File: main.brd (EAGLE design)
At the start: 42.9 x 27.9 mm, 46 parts, among them IC1 MEGA8-AI, IC2 MCP73831, IC3 7805DT, Q2 32768k

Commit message: Firmware
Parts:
- moved R12 86.6 mm to (34.3, 19.1)
- moved R14 82.4 mm to (21.6, 24.1), turned to 180 degrees
- moved T5 80.7 mm to (30.5, 17.1), turned to 180 degrees
- moved R15 75.6 mm to (5.08, 15.2), turned to 270 degrees
- moved T4 73.2 mm to (26.7, 17.8), turned to 180 degrees
- moved R11 70.4 mm to (21.6, 19.1), turned to 180 degrees
- moved R13 65.9 mm to (8.89, 24.1)
- moved R18 56.7 mm to (21.6, 26.7), turned to 180 degrees
- moved R16 55.8 mm to (21.6, 16.5)
- moved R19 52.6 mm to (11.4, 26.7)
- moved R17 48.6 mm to (16.5, 26.7), turned to 180 degrees
- turned T6 to 90 degrees
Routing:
- net N$5: track 0.00 -> 5.61 mm

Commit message: Schematics
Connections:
- net N$38: now also IC1.19; no longer IC1.12
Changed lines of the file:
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@@
 </signal>
 <signal name="N$38">
-<contactref element="IC1" pad="12"/>
 <contactref element="R22" pad="1"/>
 <contactref element="S1" pad="1"/>
+<contactref element="IC1" pad="19"/>
+<wire x1="3.0988" y1="11.1506" x2="23.565" y2="2.0574" width="0" layer="19" extent="1-1"/>
 <wire x1="-42.062" y1="58.42" x2="3.0988" y2="11.1506" width="0" layer="19" extent="1-1"/>
-<wire x1="20.4724" y1="6.75" x2="3.0988" y2="11.1506" width="0" layer="19" extent="1-1"/>
 </signal>
 <signal name="N$5">

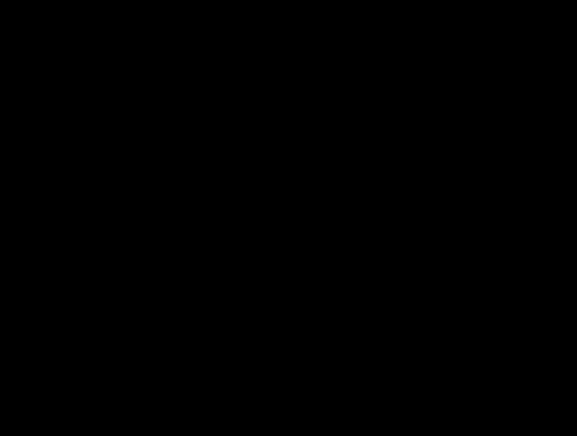
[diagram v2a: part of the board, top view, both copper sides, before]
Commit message: Button noise rejection
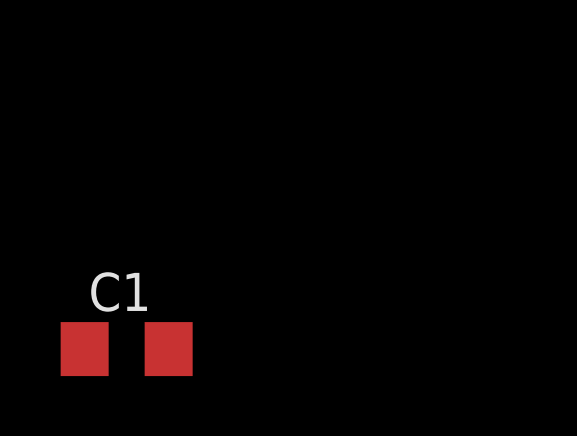
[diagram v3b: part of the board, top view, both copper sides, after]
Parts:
- added C1: 100n, rcl:C1206
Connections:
- net GND: now also C1.2
- net N$38: now also C1.1
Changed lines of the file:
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@@
 </element>
 <element name="D4" library="diode" package="D-7.5" value="" x="31.75" y="6.35" rot="R270"/>
+<element name="C1" library="rcl" package="C1206" value="100n" x="-57.15" y="-5.08"/>
 </elements>
 <signals>
@@
 <contactref element="D2" pad="A"/>
 <contactref element="S1" pad="3"/>
-<wire x1="35.56" y1="2.54" x2="3.0988" y2="6.6294" width="0" layer="19" extent="1-1"/>
-<wire x1="-45.72" y1="27.94" x2="35.56" y2="2.54" width="0" layer="19" extent="1-1"/>
+<contactref element="C1" pad="2"/>
+<wire x1="-45.72" y1="27.94" x2="-55.75" y2="-5.08" width="0" layer="19" extent="1-1"/>
 <wire x1="-38.1" y1="26.64" x2="-45.72" y2="27.94" width="0" layer="19" extent="1-1"/>
-<wire x1="14.605" y1="10.6934" x2="-38.1" y2="26.64" width="0" layer="19" extent="1-1"/>
-<wire x1="-54.48" y1="38.1" x2="35.56" y2="2.54" width="0" layer="19" extent="1-1"/>
-<wire x1="-48.13" y1="38.1" x2="-54.48" y2="38.1" width="0" layer="19" extent="1-1"/>
-<wire x1="34.795" y1="8.255" x2="-48.13" y2="38.1" width="0" layer="19" extent="1-1"/>
-<wire x1="0.27" y1="24.4" x2="34.795" y2="8.255" width="0" layer="19" extent="1-1"/>
-<wire x1="-43.332" y1="45.72" x2="34.795" y2="8.255" width="0" layer="19" extent="1-1"/>
-<wire x1="-30.35" y1="45.72" x2="0.27" y2="24.4" width="0" layer="19" extent="1-1"/>
+<wire x1="-48.13" y1="38.1" x2="-45.72" y2="27.94" width="0" layer="19" extent="1-1"/>
+<wire x1="-54.48" y1="38.1" x2="-48.13" y2="38.1" width="0" layer="19" extent="1-1"/>
+<wire x1="-43.332" y1="45.72" x2="-48.13" y2="38.1" width="0" layer="19" extent="1-1"/>
+<wire x1="-30.35" y1="45.72" x2="-43.332" y2="45.72" width="0" layer="19" extent="1-1"/>
 <wire x1="-25.27" y1="45.72" x2="-30.35" y2="45.72" width="0" layer="19" extent="1-1"/>
 <wire x1="-20.19" y1="45.72" x2="-25.27" y2="45.72" width="0" layer="19" extent="1-1"/>
-<wire x1="39.64" y1="7.255" x2="-25.27" y2="45.72" width="0" layer="19" extent="1-1"/>
 <wire x1="-36.982" y1="58.42" x2="-43.332" y2="45.72" width="0" layer="19" extent="1-1"/>
-<wire x1="20.36" y1="3.81" x2="14.605" y2="10.6934" width="0" layer="19" extent="1-1"/>
-<wire x1="25.165" y1="2.0574" x2="20.36" y2="3.81" width="0" layer="19" extent="1-1"/>
-<wire x1="24.365" y1="10.6426" x2="25.165" y2="2.0574" width="0" layer="19" extent="1-1"/>
+<wire x1="0.27" y1="24.4" x2="-20.19" y2="45.72" width="0" layer="19" extent="1-1"/>
+<wire x1="3.0988" y1="6.6294" x2="0.27" y2="24.4" width="0" layer="19" extent="1-1"/>
+<wire x1="14.605" y1="10.6934" x2="3.0988" y2="6.6294" width="0" layer="19" extent="1-1"/>
+<wire x1="20.36" y1="3.81" x2="14.605" y2="10.6934" width="0" layer="19" extent="1-16"/>
+<wire x1="25.165" y1="2.0574" x2="20.36" y2="3.81" width="0" layer="19" extent="1-16"/>
+<wire x1="24.365" y1="10.6426" x2="20.36" y2="3.81" width="0" layer="19" extent="1-16"/>
 <wire x1="25.965" y1="10.6426" x2="24.365" y2="10.6426" width="0" layer="19" extent="1-1"/>
+<wire x1="34.795" y1="8.255" x2="25.965" y2="10.6426" width="0" layer="19" extent="1-1"/>
+<wire x1="39.64" y1="7.255" x2="34.795" y2="8.255" width="0" layer="19" extent="1-1"/>
+<wire x1="35.56" y1="2.54" x2="34.795" y2="8.255" width="0" layer="19" extent="1-1"/>
 </signal>
 <signal name="+5V">
@@
 <contactref element="S1" pad="1"/>
 <contactref element="IC1" pad="19"/>
-<wire x1="3.0988" y1="11.1506" x2="23.565" y2="2.0574" width="0" layer="19" extent="1-1"/>
+<contactref element="C1" pad="1"/>
+<wire x1="3.0988" y1="11.1506" x2="-58.55" y2="-5.08" width="0" layer="19" extent="1-1"/>
+<wire x1="23.565" y1="2.0574" x2="3.0988" y2="11.1506" width="0" layer="19" extent="1-1"/>
 <wire x1="-42.062" y1="58.42" x2="3.0988" y2="11.1506" width="0" layer="19" extent="1-1"/>
 </signal>

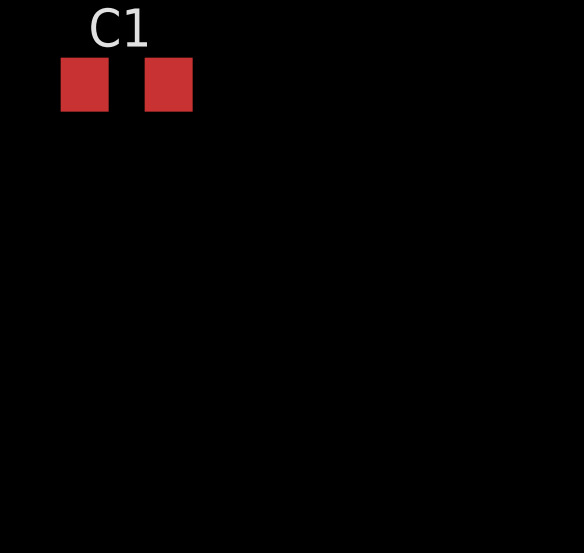
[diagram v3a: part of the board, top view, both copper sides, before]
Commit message: Pull-up resistors on TWI bus
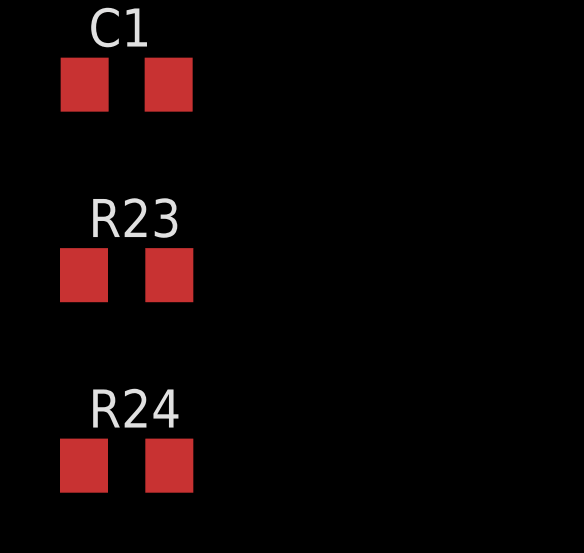
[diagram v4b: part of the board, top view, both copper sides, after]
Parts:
- added R23, R24: 4.7k, rcl:R1206
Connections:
- net +5V: now also R23.2, R24.2
- net DS1629_SCL: now also R24.1
- net DS1629_SDA: now also R23.1
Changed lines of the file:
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@@
 <element name="D4" library="diode" package="D-7.5" value="" x="31.75" y="6.35" rot="R270"/>
 <element name="C1" library="rcl" package="C1206" value="100n" x="-57.15" y="-5.08"/>
+<element name="R23" library="rcl" package="R1206" value="4.7k" x="-57.15" y="-11.43"/>
+<element name="R24" library="rcl" package="R1206" value="4.7k" x="-57.15" y="-17.78"/>
 </elements>
 <signals>
@@
 <contactref element="IC1" pad="18"/>
 <contactref element="R22" pad="2"/>
-<wire x1="-19.37" y1="62.4" x2="-14.29" y2="62.4" width="0" layer="19" extent="1-1"/>
-<wire x1="-24.45" y1="62.4" x2="-19.37" y2="62.4" width="0" layer="19" extent="1-1"/>
-<wire x1="25.72" y1="18.88" x2="-24.45" y2="62.4" width="0" layer="19" extent="1-1"/>
-<wire x1="29.53" y1="18.245" x2="25.72" y2="18.88" width="0" layer="19" extent="1-1"/>
-<wire x1="-39.218" y1="58.42" x2="29.53" y2="18.245" width="0" layer="19" extent="1-1"/>
-<wire x1="20.168" y1="19.05" x2="-39.218" y2="58.42" width="0" layer="19" extent="1-1"/>
-<wire x1="-34.138" y1="52.07" x2="20.168" y2="19.05" width="0" layer="19" extent="1-1"/>
+<contactref element="R23" pad="2"/>
+<contactref element="R24" pad="2"/>
+<wire x1="-55.728" y1="-11.43" x2="-55.728" y2="-17.78" width="0" layer="19" extent="1-1"/>
+<wire x1="-37.15" y1="29.24" x2="-55.728" y2="-11.43" width="0" layer="19" extent="1-1"/>
+<wire x1="-50.93" y1="38.1" x2="-37.15" y2="29.24" width="0" layer="19" extent="1-1"/>
+<wire x1="-57.28" y1="38.1" x2="-50.93" y2="38.1" width="0" layer="19" extent="1-1"/>
+<wire x1="-34.138" y1="52.07" x2="-50.93" y2="38.1" width="0" layer="19" extent="1-1"/>
 <wire x1="-29.058" y1="52.07" x2="-34.138" y2="52.07" width="0" layer="19" extent="1-1"/>
 <wire x1="-23.978" y1="52.07" x2="-29.058" y2="52.07" width="0" layer="19" extent="1-1"/>
-<wire x1="35.712" y1="19.05" x2="20.168" y2="19.05" width="0" layer="19" extent="1-1"/>
-<wire x1="-50.93" y1="38.1" x2="35.712" y2="19.05" width="0" layer="19" extent="1-1"/>
-<wire x1="-57.28" y1="38.1" x2="-50.93" y2="38.1" width="0" layer="19" extent="1-1"/>
-<wire x1="-37.15" y1="29.24" x2="-50.93" y2="38.1" width="0" layer="19" extent="1-1"/>
-<wire x1="25.165" y1="10.6426" x2="-37.15" y2="29.24" width="0" layer="19" extent="1-1"/>
+<wire x1="-39.218" y1="58.42" x2="-34.138" y2="52.07" width="0" layer="19" extent="1-1"/>
+<wire x1="-24.45" y1="62.4" x2="-23.978" y2="52.07" width="0" layer="19" extent="1-1"/>
+<wire x1="-19.37" y1="62.4" x2="-24.45" y2="62.4" width="0" layer="19" extent="1-1"/>
+<wire x1="-14.29" y1="62.4" x2="-19.37" y2="62.4" width="0" layer="19" extent="1-1"/>
+<wire x1="20.168" y1="19.05" x2="-23.978" y2="52.07" width="0" layer="19" extent="1-1"/>
+<wire x1="25.72" y1="18.88" x2="20.168" y2="19.05" width="0" layer="19" extent="1-1"/>
+<wire x1="29.53" y1="18.245" x2="25.72" y2="18.88" width="0" layer="19" extent="1-1"/>
+<wire x1="35.712" y1="19.05" x2="29.53" y2="18.245" width="0" layer="19" extent="1-1"/>
+<wire x1="25.165" y1="10.6426" x2="25.72" y2="18.88" width="0" layer="19" extent="1-1"/>
 <wire x1="23.565" y1="10.6426" x2="25.165" y2="10.6426" width="0" layer="19" extent="1-1"/>
 <wire x1="29.0576" y1="6.75" x2="25.165" y2="10.6426" width="0" layer="19" extent="1-1"/>
-<wire x1="24.365" y1="2.0574" x2="29.0576" y2="6.75" width="0" layer="19" extent="1-1"/>
+<wire x1="27.66" y1="1.53" x2="29.0576" y2="6.75" width="0" layer="19" extent="1-16"/>
+<wire x1="24.365" y1="2.0574" x2="27.66" y2="1.53" width="0" layer="19" extent="1-16"/>
 <wire x1="22.765" y1="2.0574" x2="24.365" y2="2.0574" width="0" layer="19" extent="1-1"/>
-<wire x1="27.66" y1="1.53" x2="22.765" y2="2.0574" width="0" layer="19" extent="1-1"/>
 </signal>
 <signal name="N$8">
@@
 <contactref element="U$1" pad="1"/>
 <contactref element="IC1" pad="27"/>
-<wire x1="18.415" y1="10.6934" x2="29.0576" y2="5.15" width="0" layer="19" extent="1-1"/>
+<contactref element="R23" pad="1"/>
+<wire x1="18.415" y1="10.6934" x2="-58.572" y2="-11.43" width="0" layer="19" extent="1-1"/>
+<wire x1="29.0576" y1="5.15" x2="18.415" y2="10.6934" width="0" layer="19" extent="1-1"/>
 </signal>
 <signal name="DS1629_SCL">
 <contactref element="U$1" pad="2"/>
 <contactref element="IC1" pad="28"/>
-<wire x1="17.145" y1="10.6934" x2="29.0576" y2="5.95" width="0" layer="19" extent="1-1"/>
+<contactref element="R24" pad="1"/>
+<wire x1="17.145" y1="10.6934" x2="-58.572" y2="-17.78" width="0" layer="19" extent="1-1"/>
+<wire x1="29.0576" y1="5.95" x2="17.145" y2="10.6934" width="0" layer="19" extent="1-1"/>
 </signal>
 <signal name="N$28">

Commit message: Remove MCU external clock, use internal RC 4 MHz
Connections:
- removed net MCU_CLOCK: IC1.7, U$1.7
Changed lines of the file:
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@@
 <wire x1="12.7" y1="1.27" x2="14.605" y2="4.5466" width="0" layer="19" extent="1-1"/>
-</signal>
-<signal name="MCU_CLOCK">
-<contactref element="IC1" pad="7"/>
-<contactref element="U$1" pad="7"/>
-<wire x1="17.145" y1="4.5466" x2="22.765" y2="10.6426" width="0" layer="19" extent="1-1"/>
 </signal>
 <signal name="VDD">

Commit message: Move display pins to make debug pin
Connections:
- net N$19: now also IC1.9; no longer IC1.2
- net N$21: now also IC1.32; no longer IC1.31
- net N$22: now also IC1.1; no longer IC1.32
- net N$30: now also IC1.2; no longer IC1.1
- net N$35: now also IC1.10; no longer IC1.9
- net N$36: now also IC1.11; no longer IC1.10
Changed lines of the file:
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@@
 <signal name="N$21">
 <contactref element="R14" pad="1"/>
-<contactref element="IC1" pad="31"/>
-<wire x1="23.012" y1="24.13" x2="29.0576" y2="8.35" width="0" layer="19" extent="1-1"/>
+<contactref element="IC1" pad="32"/>
+<wire x1="29.0576" y1="9.15" x2="23.012" y2="24.13" width="0" layer="19" extent="1-1"/>
 </signal>
 <signal name="N$22">
 <contactref element="R15" pad="1"/>
-<contactref element="IC1" pad="32"/>
-<wire x1="5.08" y1="16.662" x2="29.0576" y2="9.15" width="0" layer="19" extent="1-1"/>
+<contactref element="IC1" pad="1"/>
+<wire x1="5.08" y1="16.662" x2="27.565" y2="10.6426" width="0" layer="19" extent="1-1"/>
 </signal>
 <signal name="N$30">
 <contactref element="R16" pad="1"/>
-<contactref element="IC1" pad="1"/>
-<wire x1="27.565" y1="10.6426" x2="20.168" y2="16.51" width="0" layer="19" extent="1-1"/>
+<contactref element="IC1" pad="2"/>
+<wire x1="20.168" y1="16.51" x2="26.765" y2="10.6426" width="0" layer="19" extent="1-1"/>
 </signal>
 <signal name="N$31">
@@
 <signal name="N$19">
 <contactref element="R17" pad="1"/>
-<contactref element="IC1" pad="2"/>
-<wire x1="26.765" y1="10.6426" x2="17.932" y2="26.67" width="0" layer="19" extent="1-1"/>
+<contactref element="IC1" pad="9"/>
+<wire x1="20.4724" y1="9.15" x2="17.932" y2="26.67" width="0" layer="19" extent="1-1"/>
 </signal>
 <signal name="N$35">
 <contactref element="R18" pad="1"/>
-<contactref element="IC1" pad="9"/>
-<wire x1="20.4724" y1="9.15" x2="23.012" y2="26.67" width="0" layer="19" extent="1-1"/>
+<contactref element="IC1" pad="10"/>
+<wire x1="20.4724" y1="8.35" x2="23.012" y2="26.67" width="0" layer="19" extent="1-1"/>
 </signal>
 <signal name="N$36">
 <contactref element="R19" pad="1"/>
-<contactref element="IC1" pad="10"/>
-<wire x1="20.4724" y1="8.35" x2="10.008" y2="26.67" width="0" layer="19" extent="1-1"/>
+<contactref element="IC1" pad="11"/>
+<wire x1="20.4724" y1="7.55" x2="10.008" y2="26.67" width="0" layer="19" extent="1-1"/>
 </signal>
 <signal name="N$37">

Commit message: Change resistors/capacitors packages from 1206 to 0805
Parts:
- removed C9: 12p, rcl:C1206
- added C4: 0.1u, rcl:C0805
- C1, C8: device rcl:C1206 -> rcl:C0805
- C5: value 0.1u -> 12p; device rcl:C1206 -> rcl:C0805
- R1: device rcl:M1206 -> rcl:M0805
- R10, R11, R12, R13, R14, R15, R16, R17, R18, R19, R2, R20, R21, R22, R23, R24, R3, R4, R5, R6, R7, R8, R9: device rcl:R1206 -> rcl:M0805
- moved R19 214.5 mm to (-57.1, -176.5)
- moved R18 212.0 mm to (-57.1, -170.2), turned to 0 degrees
- moved R17 204.2 mm to (-57.1, -163.8), turned to 0 degrees
- moved R16 191.0 mm to (-57.1, -157.5)
- moved R7 187.8 mm to (-57.1, -132.1)
- moved R14 186.4 mm to (-57.1, -144.8), turned to 0 degrees
- moved C1 184.1 mm to (-57.1, -189.2)
- moved R6 182.7 mm to (-57.1, -125.7)
- moved R15 177.6 mm to (-57.1, -151.1), turned to 0 degrees
- moved R13 175.5 mm to (-57.1, -138.4)
- moved R5 165.1 mm to (-57.1, -119.4)
- moved R4 158.8 mm to (-57.1, -113.0)
- moved R3 152.7 mm to (-57.1, -106.7)
- moved R12 150.4 mm to (-57.1, -100.3)
- moved R10 141.4 mm to (-57.1, -87.6)
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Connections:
- net +5V: now also C4.1; no longer C5.1
- net GND: now also C4.2; no longer C9.2
- net N$28: now also C5.1; no longer C8.1
- net N$29: now also C8.1; no longer C9.1
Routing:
- net N$5: track 5.61 -> 0.00 mm

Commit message: Swap PB3<=>PB5
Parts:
- moved C4 235.0 mm to (22.9, 25.4)
- moved C1 234.1 mm to (34.9, 26.0)
- moved R19 193.7 mm to (14.3, 3.50), flipped to the bottom, turned to 90 degrees
- moved R18 189.5 mm to (16.5, 4.45), flipped to the bottom, turned to 90 degrees
- moved R17 182.2 mm to (12.1, 4.76), flipped to the bottom, turned to 90 degrees
- moved R7 174.0 mm to (30.1, 18.4), flipped to the bottom, turned to 90 degrees
- moved R16 173.2 mm to (9.21, 2.54), flipped to the bottom, turned to 90 degrees
- moved R14 168.5 mm to (7.62, 10.8)
- moved R15 166.4 mm to (6.65, 2.54), turned to 90 degrees
- moved R13 159.8 mm to (9.21, 6.99), flipped to the bottom, turned to 90 degrees
- moved R5 156.5 mm to (17.2, 18.4), flipped to the bottom, turned to 90 degrees
- moved R6 153.7 mm to (15.9, 9.53), flipped to the bottom, turned to 90 degrees
- moved R12 148.2 mm to (32.4, 17.8), flipped to the bottom, turned to 270 degrees
- moved R4 144.4 mm to (24.1, 6.35), flipped to the bottom, turned to 180 degrees
- moved R11 138.6 mm to (24.8, 17.8), flipped to the bottom, turned to 270 degrees
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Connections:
- net N$25: now also IC1.17; no longer IC1.15
- net N$27: now also IC1.15; no longer IC1.17
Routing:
- net N$34: track 0.00 -> 15.3 mm
- net N$31: track 0.00 -> 14.6 mm
- net N$2: track 0.00 -> 13.5 mm
- net N$18: track 0.00 -> 12.9 mm
- net N$19: track 0.00 -> 10.5 mm, vias 0 -> 1
- net N$21: track 0.00 -> 9.98 mm
- net DS1629_SCL: track 0.00 -> 7.58 mm, vias 0 -> 1
- net N$35: track 0.00 -> 4.85 mm, vias 0 -> 1
- net DS1629_SDA: track 0.00 -> 4.73 mm, vias 0 -> 1
- net N$22: track 0.00 -> 4.09 mm
- net N$30: track 0.00 -> 4.05 mm, vias 0 -> 1
- net N$1: track 0.00 -> 3.70 mm
- net +5V: track 0.00 -> 2.54 mm
